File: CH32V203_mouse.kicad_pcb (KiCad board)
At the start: 4 copper layers, 38 x 28 mm, 30 parts, among them J1 USB_C_Receptacle_USB2.0_16P_u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, J2 Conn_01x05_Pin, J3 Conn_01x04_Pin, SW1 SW_Push, U1 CH32V203G6U6, U2 USBLC6-2SC6, U3 XC6206P332MR, X1 16MHz

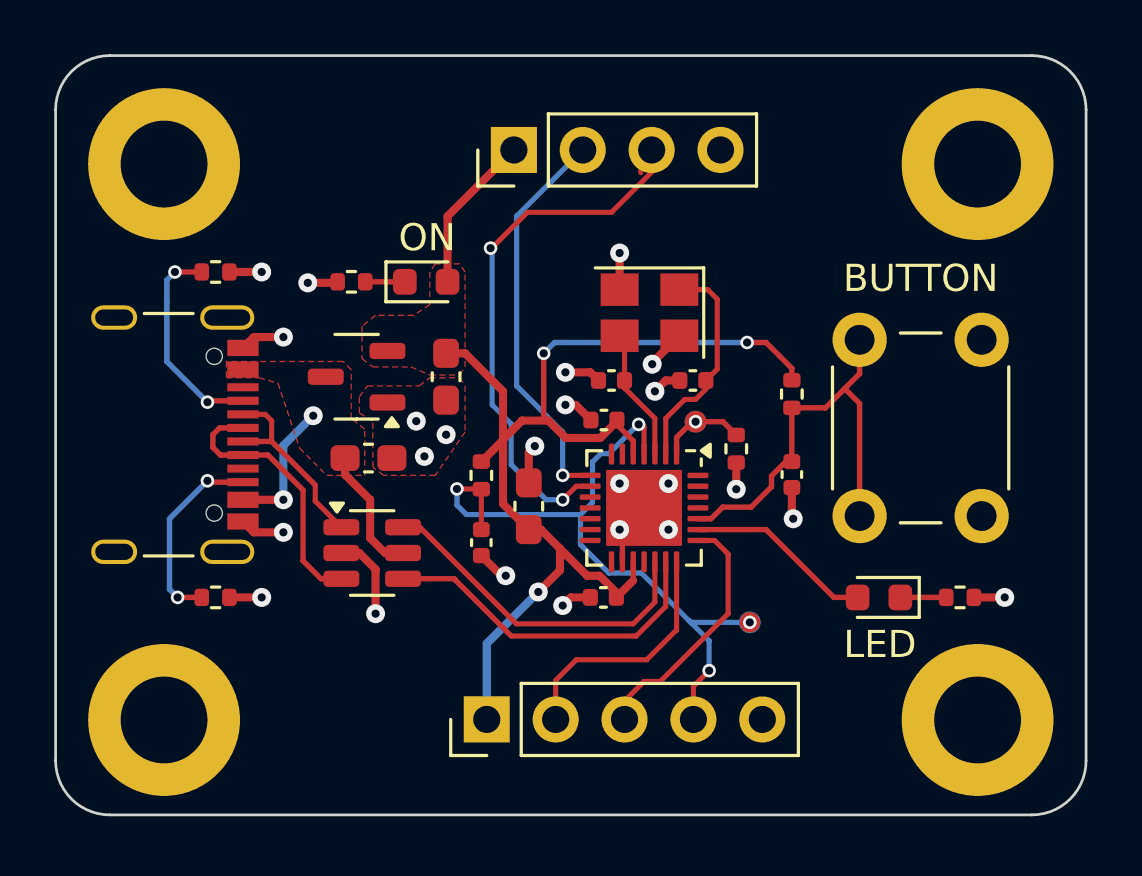
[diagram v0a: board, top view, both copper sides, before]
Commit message: Stitching vias teardrops
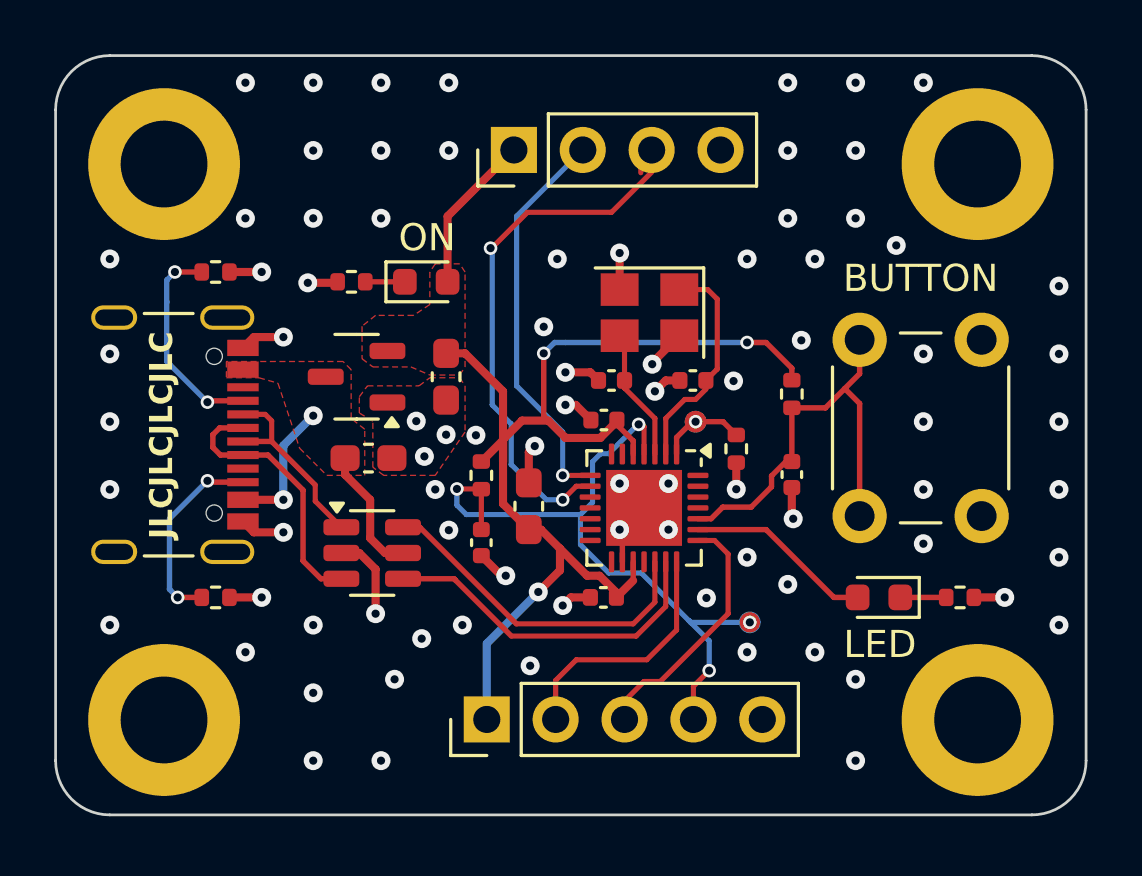
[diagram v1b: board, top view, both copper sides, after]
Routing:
- net GND: vias 24 -> 82
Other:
- board text added: "JLCJLCJLCJLC"

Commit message: Final touches making sure fabrication files are compatible with JLCPCB
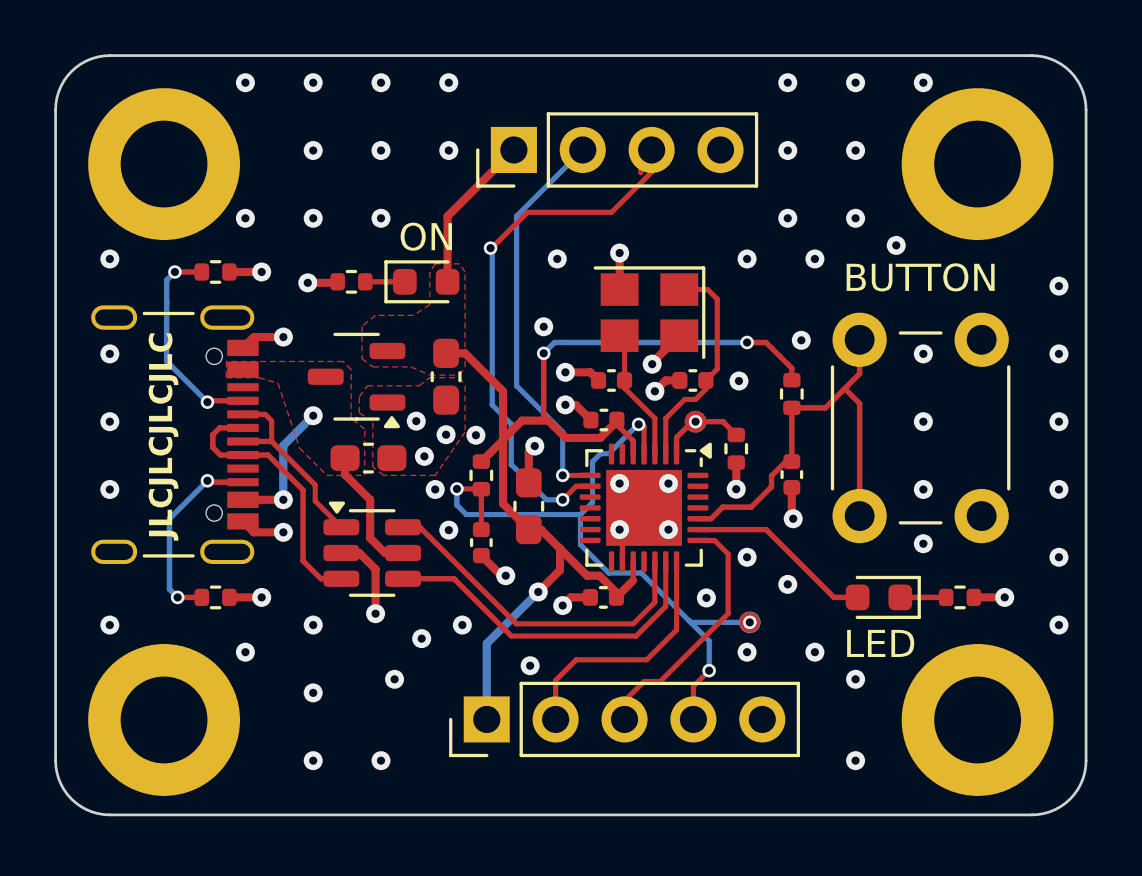
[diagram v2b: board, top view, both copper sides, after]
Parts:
- C6, C7: value 10pF -> 10p
- D1: value LED -> RED
- D2: value LED -> WHITE

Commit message: Tracks routed to the new connector
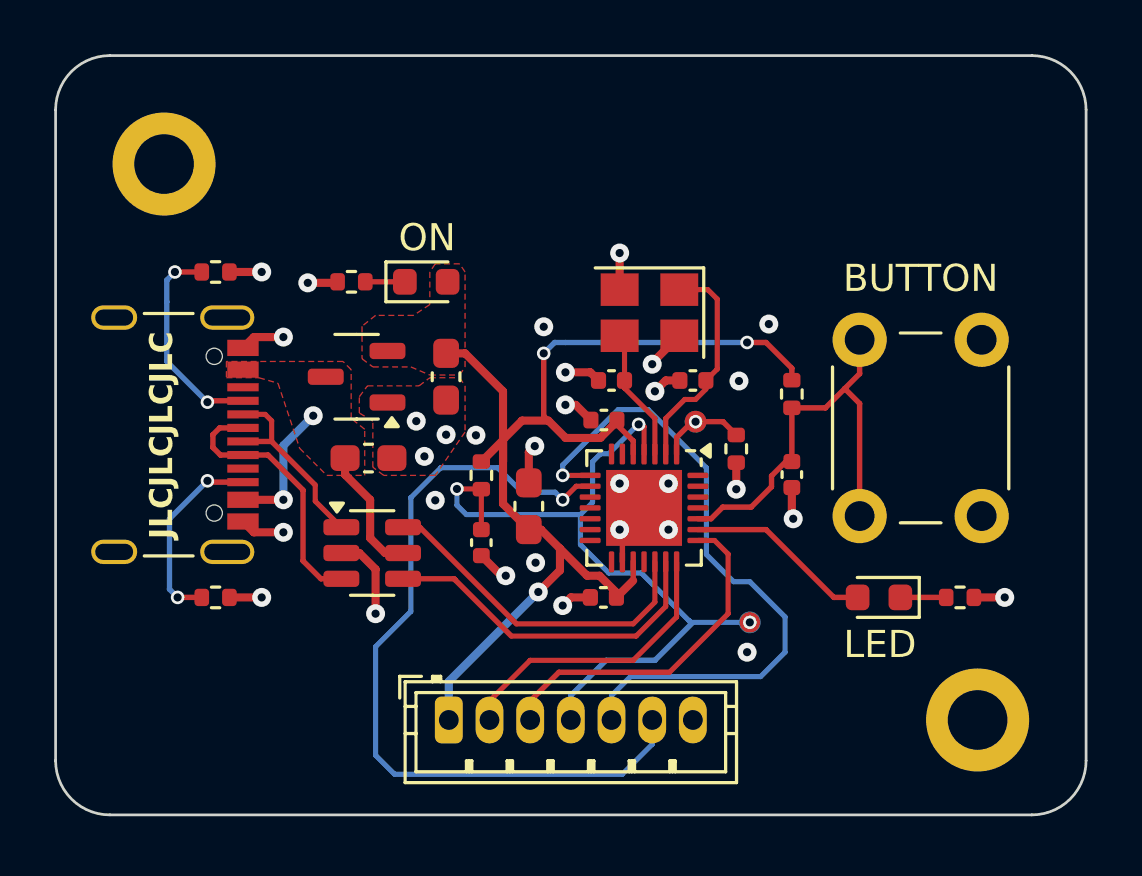
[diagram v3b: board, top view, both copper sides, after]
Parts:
- removed H3, H4: MountingHole_Pad, MountingHole:MountingHole_3.2mm_M3_DIN965_Pad
- removed J3: Conn_01x04_Pin, Connector_PinHeader_2.54mm:PinHeader_1x04_P2.54mm_Vertical
- H1, H2: footprint MountingHole:MountingHole_3.2mm_M3_DIN965_Pad -> MountingHole:MountingHole_2.2mm_M2_DIN965_Pad
- J2: value Conn_01x05_Pin -> Conn_01x07_Pin; footprint Connector_PinHeader_2.54mm:PinHeader_1x05_P2.54mm_Vertical -> Connector_JST:JST_ZH_B7B-ZR_1x07_P1.50mm_Vertical
- moved H2 20.5 mm to (152.0, 108.5)
- moved J2 1.40 mm to (132.5, 108.5), turned to 0 degrees
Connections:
- J2 pad 5: GND -> /UART_TX
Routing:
- net /UART_TX: track 14.7 -> 25.4 mm
- net /UART_RX: track 19.8 -> 29.6 mm, vias 2 -> 1
- net +3.3V: track 48.6 -> 43.3 mm
- net /SWCLK: track 9.35 -> 12.9 mm
- net /NRST: track 26.4 -> 28.7 mm, vias 4 -> 3
- net /SWDIO: track 9.18 -> 10.9 mm
- net GND: vias 82 -> 31

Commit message: Rerouted tracks
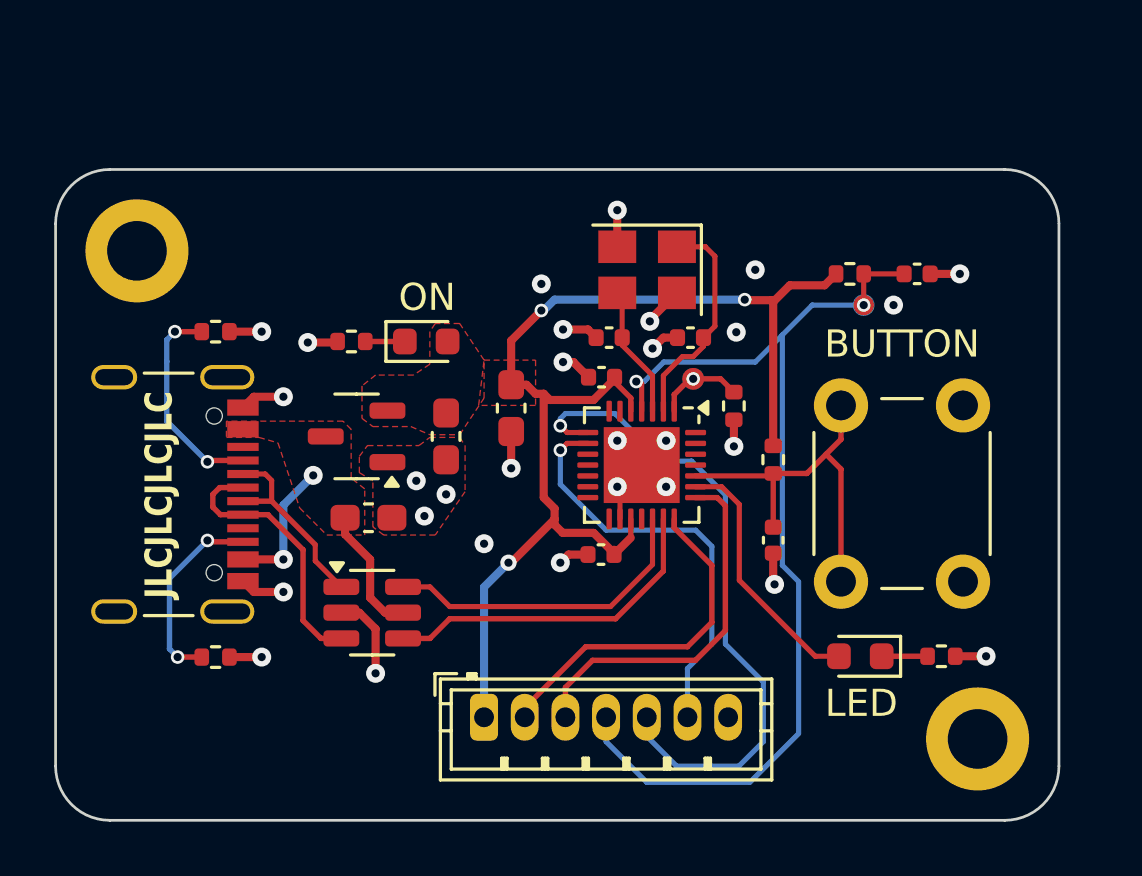
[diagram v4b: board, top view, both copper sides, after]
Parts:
- moved C9 18.9 mm to (149.8, 92.0), turned to 0 degrees
- moved R6 15.5 mm to (147.3, 92.0), turned to 0 degrees
- moved C3 3.68 mm to (134.8, 97.0), turned to -90 degrees
- moved H1 3.35 mm to (121.0, 91.2)
- moved C8 2.52 mm to (144.5, 101.9)
- moved R5 2.52 mm to (144.5, 98.9)
- moved SW1 2.52 mm to (147.0, 103.4)
- moved D2 2.28 mm to (147.7, 106.2)
- moved R4 2.28 mm to (150.7, 106.2)
- moved C1 2.20 mm to (129.5, 101.0)
- moved C2 2.20 mm to (132.4, 98.0)
- moved D1 2.20 mm to (131.7, 94.5)
- moved J1 2.20 mm to (122.4, 100.2)
- moved R1 2.20 mm to (123.9, 94.2)
- moved R2 2.20 mm to (123.9, 106.2)
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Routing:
- net /UART_RX: track 29.6 -> 15.6 mm
- net /NRST: track 28.7 -> 38.0 mm, vias 3 -> 2
- net /LED: track 6.92 -> 9.52 mm
- net /SWDIO: track 10.9 -> 12.9 mm
- net /SWITCH: track 15.8 -> 14.1 mm
- net /UART_TX: track 25.4 -> 24.4 mm
- net +3.3V: track 43.3 -> 44.3 mm
- net /SWCLK: track 12.9 -> 13.7 mm
- net /USB_DN: track 12.6 -> 11.8 mm
- net GND: track 25.8 -> 25.5 mm, vias 31 -> 29
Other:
- board size 38 x 28 mm -> 37 x 24 mm

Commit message: PCB finished some parts excluded from BOM copper pours on top and bottom layers stitching vias
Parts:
- moved C1 0.20 mm to (129.5, 100.8)
- moved C2 0.20 mm to (132.4, 97.8)
- moved C4 0.20 mm to (138.1, 95.7)
- moved C6 0.20 mm to (141.4, 94.2)
- moved C7 0.20 mm to (138.4, 94.2)
- moved C8 0.20 mm to (144.5, 101.7)
- moved D1 0.20 mm to (131.7, 94.3)
- moved H1 0.20 mm to (121.0, 91.0)
- moved H2 0.20 mm to (152.0, 109.0)
- moved R3 0.20 mm to (128.9, 94.3)
- moved R4 0.20 mm to (150.7, 106.0)
- moved R5 0.20 mm to (144.5, 98.7)
- moved R6 0.20 mm to (147.3, 91.8)
- moved R7 0.20 mm to (143.0, 96.7)
- moved SW1 0.20 mm to (147.0, 103.2)
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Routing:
- net GND: vias 29 -> 76
- added copper zone on B.Cu, net GND
